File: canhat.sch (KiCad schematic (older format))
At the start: 24 parts, among them J1 Raspberry_Pi_2_3, J2 CAN In, J3 CAN Out, U1 MCP2515-xSO, U2 MCP2551-I-SN, U3 AT24C32-SSHM, Y1 16MHz

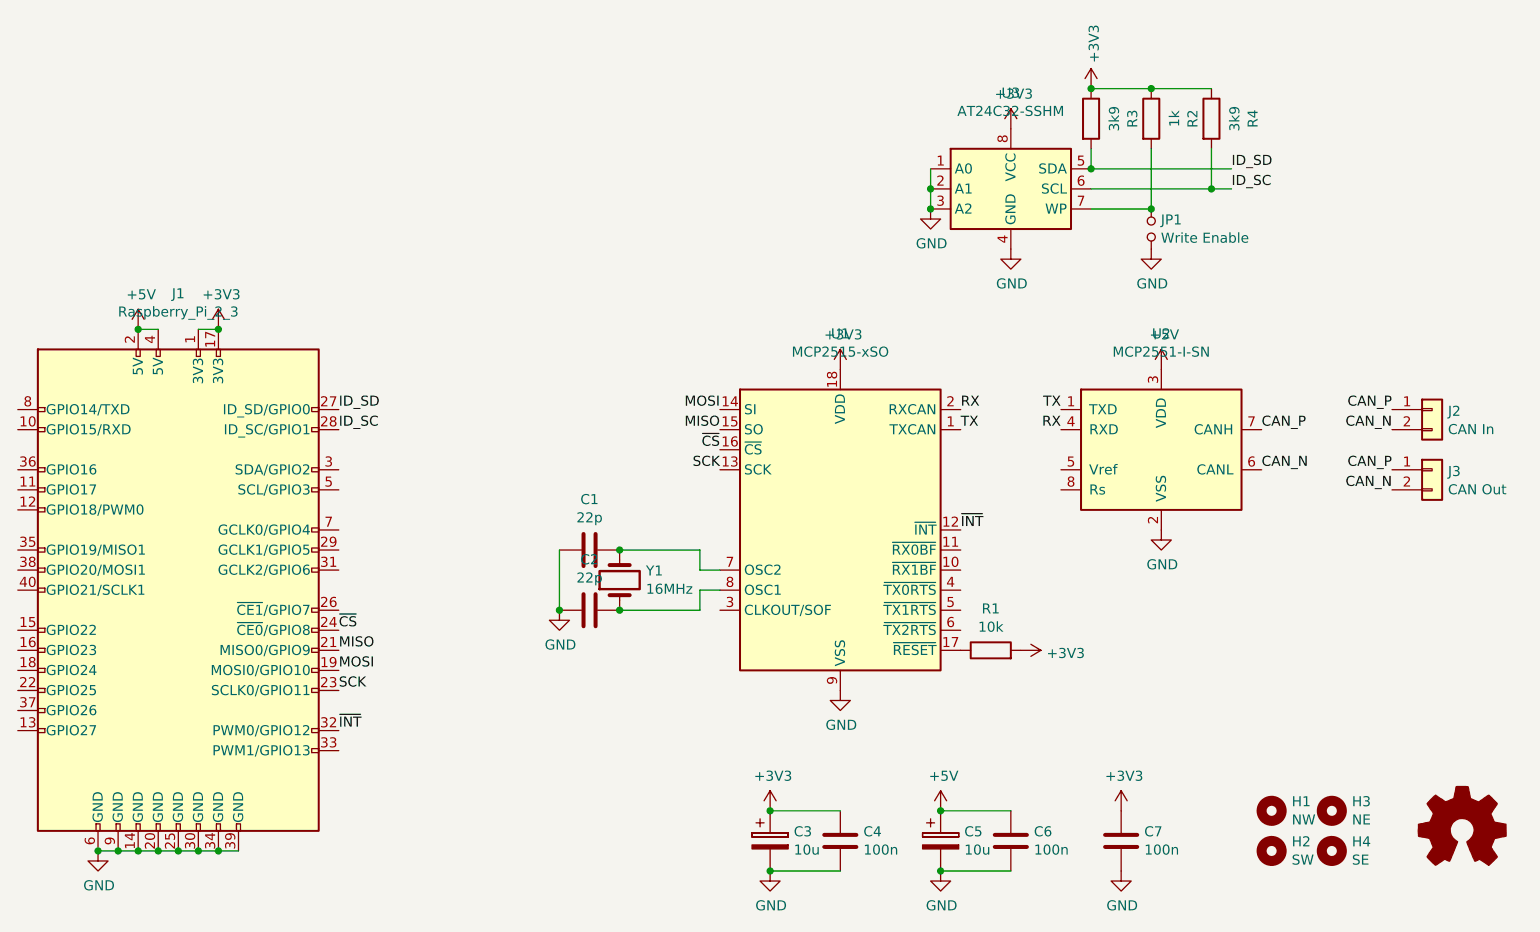
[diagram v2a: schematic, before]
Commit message: Replaced 5V parts with 3.3V and added slew control res
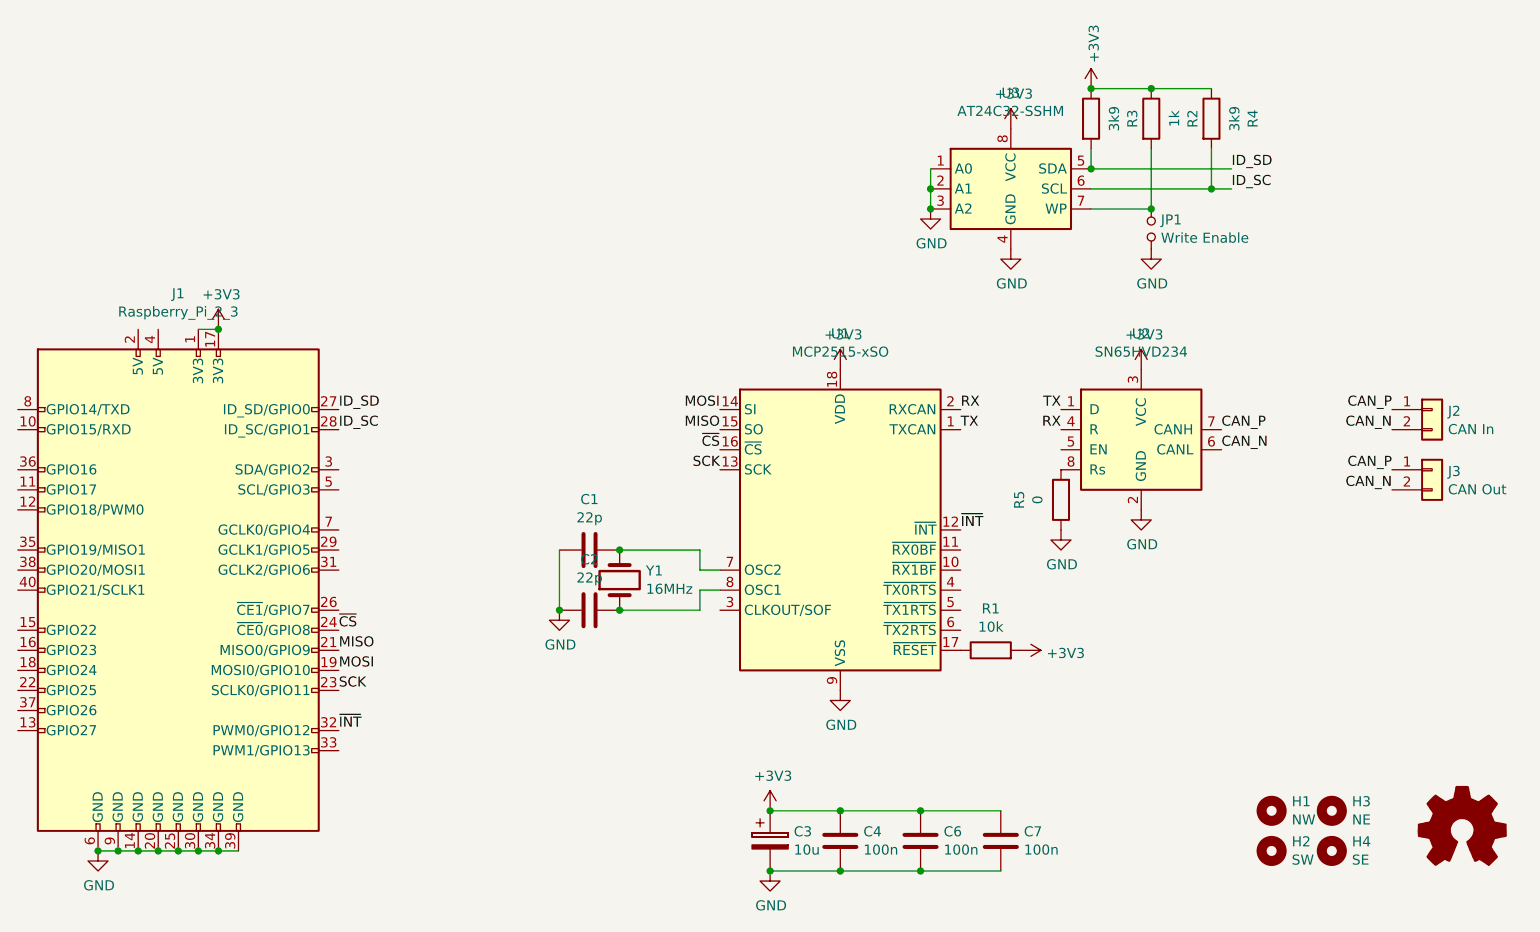
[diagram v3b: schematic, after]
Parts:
- removed C5: 10u, Capacitor_THT:CP_Radial_D5.0mm_P2.00mm, symbol Device:CP
- removed U2: MCP2551-I-SN, Package_SO:SOIC-8_3.9x4.9mm_P1.27mm, symbol Interface_CAN_LIN:MCP2551-I-SN
- added R5: 0, Resistor_SMD:R_0805_2012Metric_Pad1.15x1.40mm_HandSolder, symbol Device:R
- added U2: SN65HVD234, Package_SO:SOIC-8_3.9x4.9mm_P1.27mm, symbol Interface_CAN_LIN:SN65HVD234
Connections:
- net +3V3: now also C6.1, U2.3 (VCC)
- net CAN_N: now also U2.6 (CANL)
- net CAN_P: now also U2.7 (CANH)
- net GND: now also R5.1, U2.2 (GND)
- net RX: now also U2.4 (R)
- net TX: now also U2.1 (D)
- removed net +5V: C6.1, J1.2 (5V), J1.4 (5V)
- new net: R5.2, U2.8 (Rs)
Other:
- moved on the sheet: C6, C7
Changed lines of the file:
@@
-$EndComp
-$Comp
-L Interface_CAN_LIN:MCP2551-I-SN U2
-U 1 1 5CA27DAB
-P 8100 3400
-F 0 "U2" H 8100 3978 50  0000 C CNN
-F 1 "MCP2551-I-SN" H 8100 3887 50  0000 C CNN
-F 2 "Package_SO:SOIC-8_3.9x4.9mm_P1.27mm" H 8100 2900 50  0001 C CIN
-F 3 "http://ww1.microchip.com/downloads/en/devicedoc/21667d.pdf" H 8100 3400 50  0001 C CNN
-	1    8100 3400
-	1    0    0    -1
 $EndComp
 $Comp
@@
 L power:GND #PWR0102
 U 1 1 5CA280E2
-P 8100 3800
-F 0 "#PWR0102" H 8100 3550 50  0001 C CNN
-F 1 "GND" H 8105 3627 50  0000 C CNN
-F 2 "" H 8100 3800 50  0001 C CNN
-F 3 "" H 8100 3800 50  0001 C CNN
-	1    8100 3800
+P 8000 3700
+F 0 "#PWR0102" H 8000 3450 50  0001 C CNN
+F 1 "GND" H 8005 3527 50  0000 C CNN
+F 2 "" H 8000 3700 50  0001 C CNN
+F 3 "" H 8000 3700 50  0001 C CNN
+	1    8000 3700
 	1    0    0    -1
 $EndComp
@@
 Wire Wire Line
 	3400 5400 3500 5400
-Wire Wire Line
-	3000 2800 3100 2800
 Wire Wire Line
 	3400 2800 3300 2800
@@
 ~INT
 $Comp
-L power:+5V #PWR0108
-U 1 1 5CA2935D
-P 8100 3000
-F 0 "#PWR0108" H 8100 2850 50  0001 C CNN
-F 1 "+5V" H 8115 3173 50  0000 C CNN
-F 2 "" H 8100 3000 50  0001 C CNN
-F 3 "" H 8100 3000 50  0001 C CNN
-	1    8100 3000
-	1    0    0    -1
-$EndComp
-$Comp
-L power:+5V #PWR0109
-U 1 1 5CA293AA
-P 3000 2800
-F 0 "#PWR0109" H 3000 2650 50  0001 C CNN
-F 1 "+5V" H 3015 2973 50  0000 C CNN
-F 2 "" H 3000 2800 50  0001 C CNN
-F 3 "" H 3000 2800 50  0001 C CNN
-	1    3000 2800
-	1    0    0    -1
-$EndComp
-Connection ~ 3000 2800
-$Comp
 L Device:CP C3
 U 1 1 5CA29432
@@
 L Device:C C6
 U 1 1 5CA2998E
-P 7350 5350
-F 0 "C6" H 7465 5396 50  0000 L CNN
-F 1 "100n" H 7465 5305 50  0000 L CNN
-F 2 "Capacitor_SMD:C_0805_2012Metric_Pad1.15x1.40mm_HandSolder" H 7388 5200 50  0001 C CNN
-F 3 "~" H 7350 5350 50  0001 C CNN
-	1    7350 5350
-	1    0    0    -1
-$EndComp
-$Comp
-L power:GND #PWR0111
-U 1 1 5CA29994
-P 7000 5500
-F 0 "#PWR0111" H 7000 5250 50  0001 C CNN
-F 1 "GND" H 7005 5327 50  0000 C CNN
-F 2 "" H 7000 5500 50  0001 C CNN
-F 3 "" H 7000 5500 50  0001 C CNN
-	1    7000 5500
-	1    0    0    -1
-$EndComp
-$Comp
-L Device:CP C5
-U 1 1 5CA2999A
-P 7000 5350
-F 0 "C5" H 7118 5396 50  0000 L CNN
-F 1 "10u" H 7118 5305 50  0000 L CNN
-F 2 "Capacitor_THT:CP_Radial_D5.0mm_P2.00mm" H 7038 5200 50  0001 C CNN
-F 3 "~" H 7000 5350 50  0001 C CNN
-	1    7000 5350
-	1    0    0    -1
-$EndComp
-Wire Wire Line
-	7000 5200 7350 5200
-Wire Wire Line
-	7000 5500 7350 5500
-Connection ~ 7000 5500
-$Comp
-L power:+5V #PWR0112
-U 1 1 5CA29FA2
-P 7000 5200
-F 0 "#PWR0112" H 7000 5050 50  0001 C CNN
-F 1 "+5V" H 7015 5373 50  0000 C CNN
-F 2 "" H 7000 5200 50  0001 C CNN
-F 3 "" H 7000 5200 50  0001 C CNN
-	1    7000 5200
-	1    0    0    -1
-$EndComp
-Connection ~ 7000 5200
+P 6900 5350
+F 0 "C6" H 7015 5396 50  0000 L CNN
+F 1 "100n" H 7015 5305 50  0000 L CNN
+F 2 "Capacitor_SMD:C_0805_2012Metric_Pad1.15x1.40mm_HandSolder" H 6938 5200 50  0001 C CNN
+F 3 "~" H 6900 5350 50  0001 C CNN
+	1    6900 5350
+	1    0    0    -1
+$EndComp
 $Comp
 L power:+3V3 #PWR0113
@@
 L Device:C C7
 U 1 1 5CA2FDF9
-P 7900 5350
-F 0 "C7" H 8015 5396 50  0000 L CNN
-F 1 "100n" H 8015 5305 50  0000 L CNN
-F 2 "Capacitor_SMD:C_0805_2012Metric_Pad1.15x1.40mm_HandSolder" H 7938 5200 50  0001 C CNN
-F 3 "~" H 7900 5350 50  0001 C CNN
-	1    7900 5350
-	1    0    0    -1
-$EndComp
-$Comp
-L power:+3V3 #PWR05
-U 1 1 5CA2FE5D
-P 7900 5200
-F 0 "#PWR05" H 7900 5050 50  0001 C CNN
-F 1 "+3V3" H 7915 5373 50  0000 C CNN
-F 2 "" H 7900 5200 50  0001 C CNN
-F 3 "" H 7900 5200 50  0001 C CNN
-	1    7900 5200
-	1    0    0    -1
-$EndComp
-$Comp
-L power:GND #PWR06
-U 1 1 5CA2FE92
-P 7900 5500
-F 0 "#PWR06" H 7900 5250 50  0001 C CNN
-F 1 "GND" H 7905 5327 50  0000 C CNN
-F 2 "" H 7900 5500 50  0001 C CNN
-F 3 "" H 7900 5500 50  0001 C CNN
-	1    7900 5500
+P 7300 5350
+F 0 "C7" H 7415 5396 50  0000 L CNN
+F 1 "100n" H 7415 5305 50  0000 L CNN
+F 2 "Capacitor_SMD:C_0805_2012Metric_Pad1.15x1.40mm_HandSolder" H 7338 5200 50  0001 C CNN
+F 3 "~" H 7300 5350 50  0001 C CNN
+	1    7300 5350
 	1    0    0    -1
 $EndComp
@@
 Text Label 7100 3300 0    50   ~ 0
 TX
-Text Label 8600 3300 0    50   ~ 0
+Text Label 8400 3300 0    50   ~ 0
 CAN_P
-Text Label 8600 3500 0    50   ~ 0
+Text Label 8400 3400 0    50   ~ 0
 CAN_N
 Text Label 9250 3200 2    50   ~ 0
@@
 Text Label 9250 3600 2    50   ~ 0
 CAN_N
+$Comp
+L Interface_CAN_LIN:SN65HVD234 U2
+U 1 1 5CA3F098
+P 8000 3300
+F 0 "U2" H 8000 3778 50  0000 C CNN
+F 1 "SN65HVD234" H 8000 3687 50  0000 C CNN
+F 2 "Package_SO:SOIC-8_3.9x4.9mm_P1.27mm" H 8000 2800 50  0001 C CNN
+F 3 "http://www.ti.com/lit/ds/symlink/sn65hvd234.pdf" H 7900 3700 50  0001 C CNN
+	1    8000 3300
+	1    0    0    -1
+$EndComp
+$Comp
+L power:+3V3 #PWR0108
+U 1 1 5CA3F27F
+P 8000 3000
+F 0 "#PWR0108" H 8000 2850 50  0001 C CNN
+F 1 "+3V3" H 8015 3173 50  0000 C CNN
+F 2 "" H 8000 3000 50  0001 C CNN
+F 3 "" H 8000 3000 50  0001 C CNN
+	1    8000 3000
+	1    0    0    -1
+$EndComp
+Wire Wire Line
+	6500 5200 6900 5200
+Connection ~ 6500 5200
+Connection ~ 6900 5200
+Wire Wire Line
+	6900 5200 7300 5200
+Wire Wire Line
+	6500 5500 6900 5500
+Connection ~ 6500 5500
+Connection ~ 6900 5500
+Wire Wire Line
+	6900 5500 7300 5500
+$Comp
+L Device:R R5
+U 1 1 5CA408D1
+P 7600 3650
+F 0 "R5" V 7807 3650 50  0000 C CNN
+F 1 "0" V 7716 3650 50  0000 C CNN
+F 2 "Resistor_SMD:R_0805_2012Metric_Pad1.15x1.40mm_HandSolder" V 7530 3650 50  0001 C CNN
+F 3 "~" H 7600 3650 50  0001 C CNN
+	1    7600 3650
+	-1   0    0    1
+$EndComp
+$Comp
+L power:GND #PWR0109
+U 1 1 5CA409A5
+P 7600 3800
+F 0 "#PWR0109" H 7600 3550 50  0001 C CNN
+F 1 "GND" H 7605 3627 50  0000 C CNN
+F 2 "" H 7600 3800 50  0001 C CNN
+F 3 "" H 7600 3800 50  0001 C CNN
+	1    7600 3800
+	1    0    0    -1
+$EndComp
 $EndSCHEMATC
